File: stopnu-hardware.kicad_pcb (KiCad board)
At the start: 4 copper layers, 94 x 131 mm, 97 parts, among them CN1 SM04B-SRSS-TB (LF)(SN), CN2 OQ0232510000G, CN3 OQ0232510000G, CN4 OQ0232510000G, CN5 OQ0232510000G, CN6 OQ0432510000G, J1 Conn_02x15_Odd_Even, U1 WIFI_KIT_32__V3_, U19 SY6280AAC, U2 74HCT1G125GW-Q100H, U3 LD1117V33, U4 74HCT1G125GW-Q100H, U5 LTV-817S, U6 LTV-817S, U7 LTV-817S

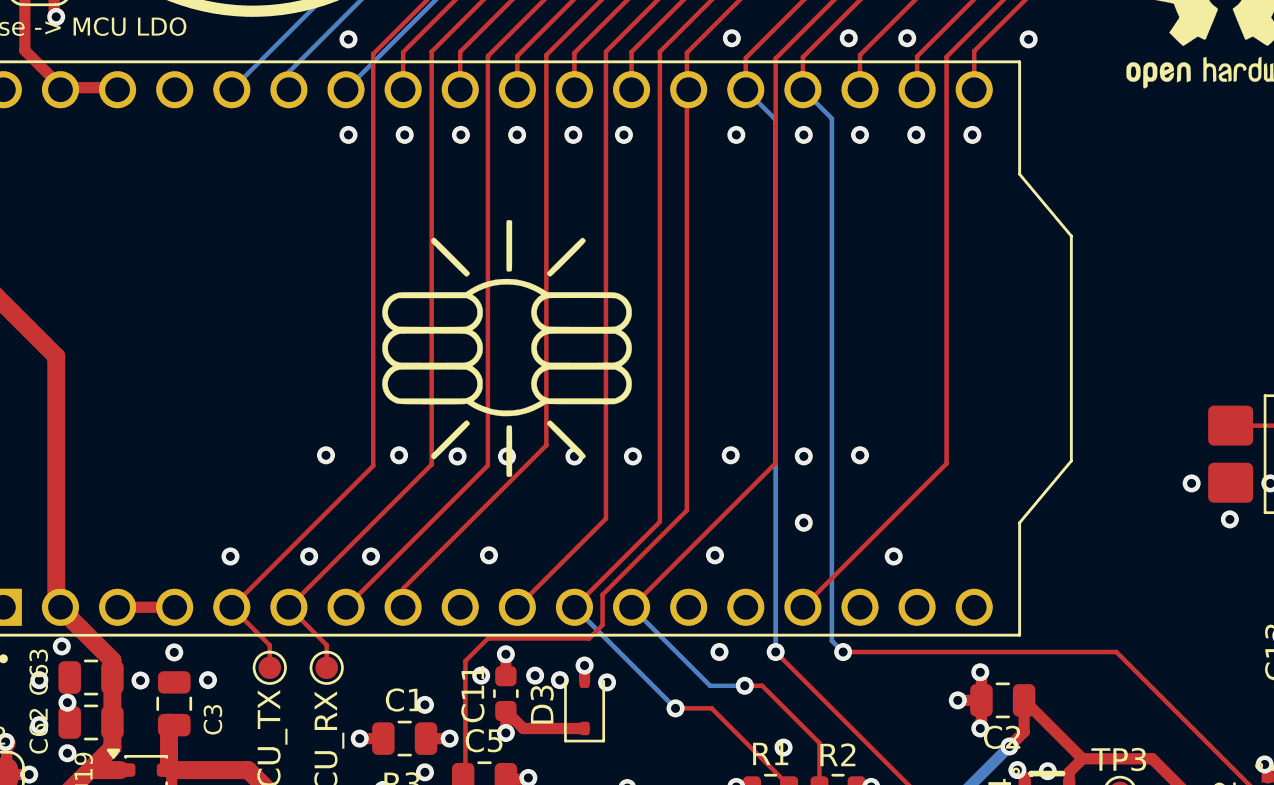
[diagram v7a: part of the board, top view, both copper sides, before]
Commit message: Add README.md, make power input more intuitive in schematic.
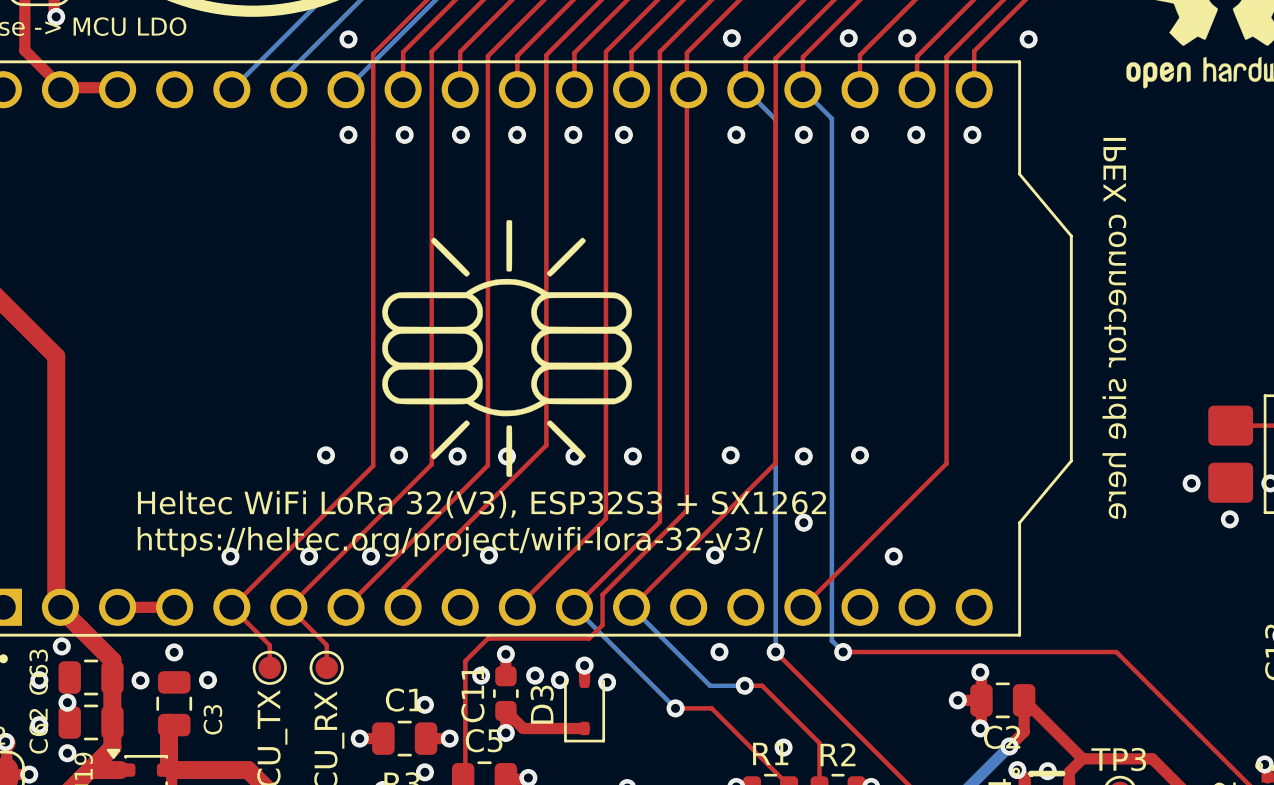
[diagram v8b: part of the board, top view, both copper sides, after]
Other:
- board text added: "Heltec WiFi LoRa 32(V3), ESP32S3 + SX1262 https://heltec.org/project/wifi-lora-32-v3/"
- board text added: "IPEX connector side here"
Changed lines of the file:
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@@
 	)
 	(footprint "kibuzzard-69470A66"
+		(locked yes)
 		(layer "F.Cu")
 		(at -6.05 -2.240914 90)
@@
 	)
 	(footprint "kibuzzard-6946CE3C"
+		(locked yes)
 		(layer "F.Cu")
 		(at -13.67 18.512329 -90)
@@
 	)
 	(footprint "kibuzzard-6946CE98"
+		(locked yes)
 		(layer "F.Cu")
 		(at 4.11 18.50685 -90)
@@
 	)
 	(footprint "lcsc:TO-220-3_L10.0-W4.5-P2.54-L"
+		(locked yes)
 		(layer "F.Cu")
 		(at -42 70.04 90)
@@
 	)
 	(footprint "kibuzzard-6946CF08"
+		(locked yes)
 		(layer "F.Cu")
 		(at 11.73 -2.259179 90)
@@
 	)
 	(footprint "kibuzzard-6946CDDB"
+		(locked yes)
 		(layer "F.Cu")
 		(at -0.97 17.821918 -90)
@@
 	)
 	(footprint "lcsc:CONN-TH_OQ0232510000G"
+		(locked yes)
 		(layer "F.Cu")
 		(at 15.0325 70.1025)
@@
 	)
 	(footprint "kibuzzard-6946CF20"
+		(locked yes)
 		(layer "F.Cu")
 		(at 6.65 -2.24685 90)
@@
 	)
 	(footprint "kibuzzard-6946CE89"
+		(locked yes)
 		(layer "F.Cu")
 		(at 9.19 18.503425 -90)
@@
 	)
 	(footprint "kibuzzard-6946CE4B"
+		(locked yes)
 		(layer "F.Cu")
 		(at -16.21 18.45 -90)
@@
 	)
 	(footprint "Package_DIP:SMDIP-4_W9.53mm"
+		(locked yes)
 		(layer "F.Cu")
 		(at 16 46.7)
@@
 	)
 	(footprint "lcsc:CONN-SMD_4P-P1.00_SM04B-SRSS-TB-LF-SN"
+		(locked yes)
 		(layer "F.Cu")
 		(at -8.8 74.5)
@@
 	)
 	(footprint "kibuzzard-69470A71"
+		(locked yes)
 		(layer "F.Cu")
 		(at -3.51 -2.285434 90)
@@
 	)
 	(footprint "kibuzzard-6946CCA1"
+		(locked yes)
 		(layer "F.Cu")
 		(at 16.8 17.5 -90)
@@
 	)
 	(footprint "kibuzzard-6946CFA1"
+		(locked yes)
 		(layer "F.Cu")
 		(at -13.67 -2.625845 90)
@@
 	)
 	(footprint "kibuzzard-6946CCA1"
+		(locked yes)
 		(layer "F.Cu")
 		(at -18.75 17.5 -90)
@@
 	)
 	(footprint "lcsc:CONN-TH_4P-P3.81_OQ0432510000G"
+		(locked yes)
 		(layer "F.Cu")
 		(at 31.245 70.135)
@@
 	)
 	(footprint "kibuzzard-69470A3B"
+		(locked yes)
 		(layer "F.Cu")
 		(at 14.27 18.502055 -90)
@@
 	)
 	(footprint "kibuzzard-6946CEFA"
+		(locked yes)
 		(layer "F.Cu")
 		(at 14.27 -2.253699 90)
@@
 	)
 	(footprint "kibuzzard-6946CE20"
+		(locked yes)
 		(layer "F.Cu")
 		(at -8.59 18.519179 -90)
@@
 	)
 	(footprint "kibuzzard-6946CEA1"
+		(locked yes)
 		(layer "F.Cu")
 		(at -3.51 18.498631 -90)
@@
 	)
 	(footprint "Package_DIP:SMDIP-4_W9.53mm"
+		(locked yes)
 		(layer "F.Cu")
 		(at 27.55 40.6)
@@
 	)
 	(footprint "Package_DIP:SMDIP-4_W9.53mm"
+		(locked yes)
 		(layer "F.Cu")
 		(at 38.95 46.85)
@@
 	)
 	(footprint "kibuzzard-6946CF95"
+		(locked yes)
 		(layer "F.Cu")
 		(at -11.13 -2.640229 90)
@@
 	)
 	(footprint "MountingHole:MountingHole_4.5mm_Pad_Via"
+		(locked yes)
 		(layer "F.Cu")
 		(at -32.25 -17)
@@
 	)
 	(footprint "MountingHole:MountingHole_4.5mm_Pad_Via"
+		(locked yes)
 		(layer "F.Cu")
 		(at -32.25 17)
@@
 	)
 	(footprint "kibuzzard-6946CF89"
+		(locked yes)
 		(layer "F.Cu")
 		(at -8.59 -2.978585 90)
@@
 	)
 	(footprint "lcsc:CONN-TH_OQ0232510000G"
+		(locked yes)
 		(layer "F.Cu")
 		(at -19.9675 70.1025)
@@
 	)
 	(footprint "kibuzzard-6946CF12"
+		(locked yes)
 		(layer "F.Cu")
 		(at 9.19 -2.242055 90)
@@
 	)
 	(footprint "kibuzzard-6946CEAD"
+		(locked yes)
 		(layer "F.Cu")
 		(at -6.05 18.45 -90)
@@
 	)
 	(footprint "footprints:StopNuVikings"
+		(locked yes)
 		(layer "F.Cu")
 		(at -1.076514 -36.027769)
@@
 	)
 	(footprint "footprints:MODULE_WIFI_KIT_32__V3_"
+		(locked yes)
 		(layer "F.Cu")
 		(at -20.95 42 90)
@@
 	)
 	(footprint "kibuzzard-6946CCA1"
+		(locked yes)
 		(layer "F.Cu")
 		(at 16.81 -1.24 90)
@@
 	)
 	(footprint "lcsc:CONN-TH_OQ0232510000G"
+		(locked yes)
 		(layer "F.Cu")
 		(at 4.0325 70.1025)
@@
 	)
 	(footprint "kibuzzard-69470A2F"
+		(locked yes)
 		(layer "F.Cu")
 		(at 11.73 18.513699 -90)
@@
 	)
 	(footprint "kibuzzard-6946CF52"
+		(locked yes)
 		(layer "F.Cu")
 		(at -0.97 -1.241142 90)
@@
 	)
 	(footprint "kibuzzard-6946CF2B"
+		(locked yes)
 		(layer "F.Cu")
 		(at 4.11 -2.238631 90)
@@
 	)
 	(footprint "footprints:goatse_01"
+		(locked yes)
 		(layer "F.Cu")
 		(at -20.95 42)
@@
 	)
 	(footprint "MountingHole:MountingHole_4.5mm_Pad_Via"
+		(locked yes)
 		(layer "F.Cu")
 		(at 32.25 -17)
@@
 	)
 	(footprint "kibuzzard-6946CFA8"
+		(locked yes)
 		(layer "F.Cu")
 		(at -16.21 -2.625845 90)
@@
 	)
 	(footprint "kibuzzard-6946CCA1"
+		(locked yes)
 		(layer "F.Cu")
 		(at 1.57 17.5 -90)
@@
 	)
 	(footprint "lcsc:CONN-TH_OQ0232510000G"
+		(locked yes)
 		(layer "F.Cu")
 		(at -30.9675 70.1025)
@@
 	)
 	(footprint "kibuzzard-6946CE2E"
+		(locked yes)
 		(layer "F.Cu")
 		(at -11.13 18.50685 -90)
@@
 	)
 	(footprint "Symbol:OSHW-Logo2_9.8x8mm_SilkScreen"
+		(locked yes)
 		(layer "F.Cu")
 		(at 11 26.7)
@@
 	)
 	(footprint "Connector_PinHeader_2.54mm:PinHeader_2x15_P2.54mm_Horizontal"
+		(locked yes)
 		(layer "F.Cu")
 		(at -18.75 14 90)
@@
 	)
 	(footprint "kibuzzard-6946CCA1"
+		(locked yes)
 		(layer "F.Cu")
 		(at 1.57 -1.24 90)
@@
 	)
 	(footprint "MountingHole:MountingHole_4.5mm_Pad_Via"
+		(locked yes)
 		(layer "F.Cu")
 		(at 32.25 17)
@@
 	)
 	(footprint "kibuzzard-6946CCA1"
+		(locked yes)
 		(layer "F.Cu")
 		(at -18.74 -1.24 90)
@@
 	)
 	(footprint "kibuzzard-6946CE92"
+		(locked yes)
 		(layer "F.Cu")
 		(at 6.65 18.526028 -90)
@@
 		)
 		(fill no)
+		(locked yes)
 		(layer "F.SilkS")
 	)
@@
 		)
 		(fill no)
+		(locked yes)
 		(layer "F.SilkS")
 	)
@@
 		)
 		(fill no)
+		(locked yes)
 		(layer "F.SilkS")
 	)
@@
 		)
 		(fill no)
+		(locked yes)
 		(layer "F.SilkS")
 	)
@@
 			(type default)
 		)
+		(locked yes)
 		(layer "Edge.Cuts")
 	)
@@
 			(type solid)
 		)
+		(locked yes)
 		(layer "Edge.Cuts")
 	)
@@
 			(type solid)
 		)
+		(locked yes)
 		(layer "Edge.Cuts")
 	)
@@
 			(type default)
 		)
+		(locked yes)
 		(layer "Edge.Cuts")
 	)
@@
 			(type solid)
 		)
+		(locked yes)
 		(layer "Edge.Cuts")
 	)
@@
 			(type solid)
 		)
+		(locked yes)
 		(layer "Edge.Cuts")
 	)
@@
 			(type solid)
 		)
+		(locked yes)
 		(layer "Edge.Cuts")
 	)
@@
 			(type solid)
 		)
+		(locked yes)
 		(layer "Edge.Cuts")
 	)
 	(gr_text "STOPNU"
+		(locked yes)
 		(at -14.625479 -10.13 0)
 		(layer "F.SilkS" knockout)
@@
 	)
 	(gr_text "2025 Badge.Team\n\nOrange_Murker, Jhaand, \nNightOwl, Ranzbak, R3nz3,\nStoneshop\n\nCERN Open hardware License"
+		(locked yes)
 		(at -45.42 5 0)
 		(layer "F.SilkS")
@@
 	)
 	(gr_text "https://github.com/badgeteam/stopnu-hardware"
+		(locked yes)
 		(at 45.45 22.8 90)
 		(layer "F.SilkS")
@@
 		)
 	)
+	(gr_text "Heltec WiFi LoRa 32(V3), ESP32S3 + SX1262\nhttps://heltec.org/project/wifi-lora-32-v3/"
+		(at -37.5 51.1 0)
+		(layer "F.SilkS")
+		(effects
+			(font
+				(size 1 1)
+				(thickness 0.15)
+			)
+			(justify left bottom)
+		)
+	)
+	(gr_text "IPEX connector side here"
+		(locked yes)
+		(at 6.7 32.5 90)
+		(layer "F.SilkS")
+		(effects
+			(font
+				(size 1 1)
+				(thickness 0.15)
+			)
+			(justify left bottom mirror)
+		)
+	)
